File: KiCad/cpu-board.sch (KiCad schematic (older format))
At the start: 56 parts, among them CON1 BARREL_JACK, J1 Conn_FT245R, SW1 SW_PUSH_SMALL, SW2 SW_PUSH_SMALL, SW3 SWITCH_INV, U1 29F040B, U10 74LS377, U11 GAL22V10, U2 68008D, U3 74LS00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

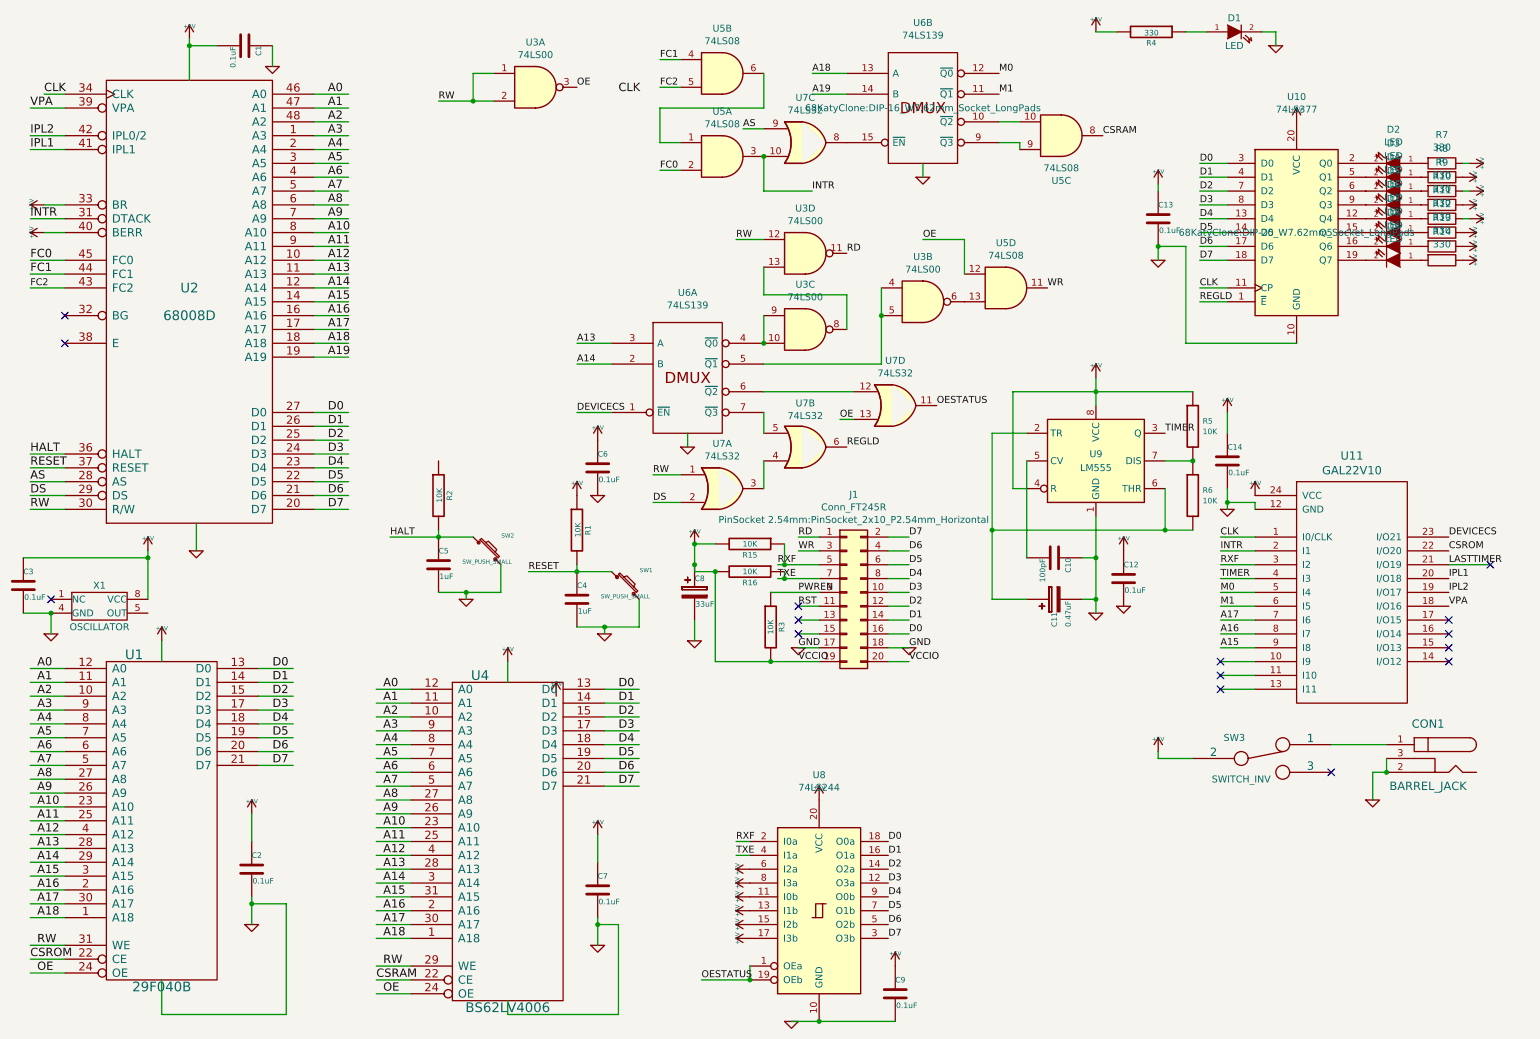
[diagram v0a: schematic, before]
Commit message: re-label active-low pins with bars
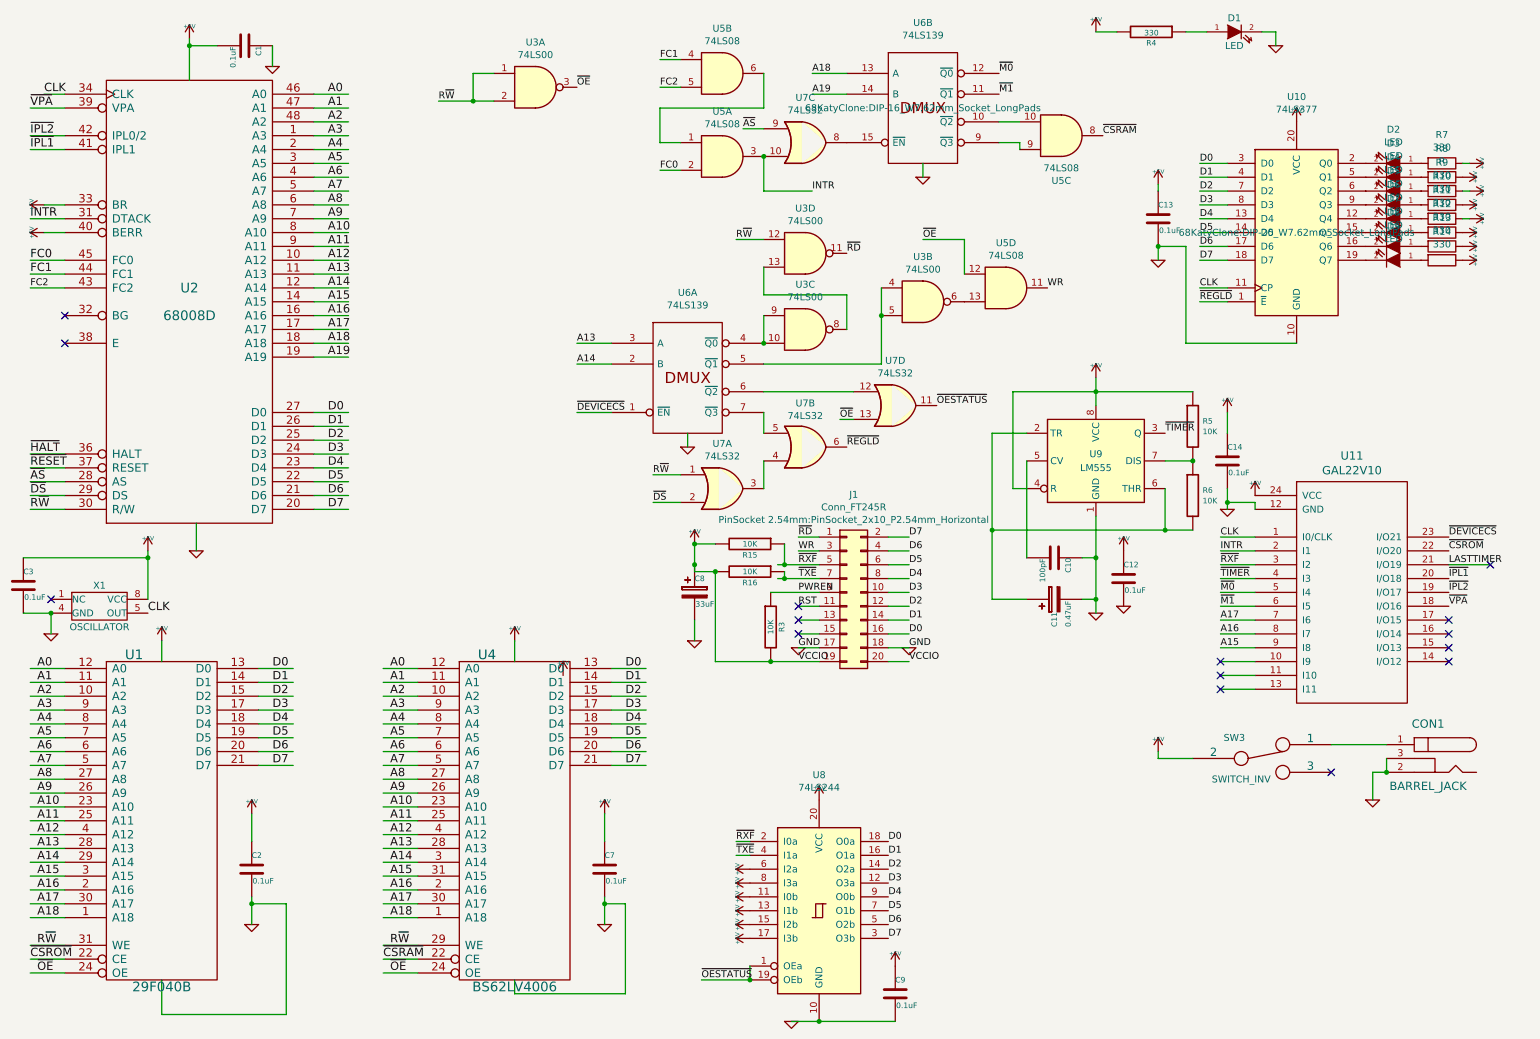
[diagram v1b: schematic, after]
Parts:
- removed C4, C5: 1uF, Discret:C1, symbol cpu-board-rescue:C
- removed C6: 0.1uF, Discret:C1, symbol cpu-board-rescue:C
- removed R1, R2: 10K, Discret:R3-5, symbol cpu-board-rescue:R
- removed SW1, SW2: SW_PUSH_SMALL, Discret:SW_PUSH_SMALL, symbol cpu-board-rescue:SW_PUSH_SMALL
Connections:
- net labels added: R~W, ~AS, ~CSRAM, ~CSROM, ~DEVICECS, ~DS, ~HALT, ~IPL1, ~IPL2, ~M0, ~M1, ~OE, ~OESTATUS, ~RD, ~REGLD, ~RESET, ~RXF, ~TIMER, ~TXE, ~VPA
- net labels removed: AS, CSRAM, CSROM, DEVICECS, DS, HALT, IPL1, IPL2, M0, M1, OE, OESTATUS, RD, REGLD, RESET, RW, RXF, TIMER, TXE, VPA
- wire segments 286 -> 272
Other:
- moved on the sheet: C7, U4

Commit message: remove data bus LEDs, they are of little use
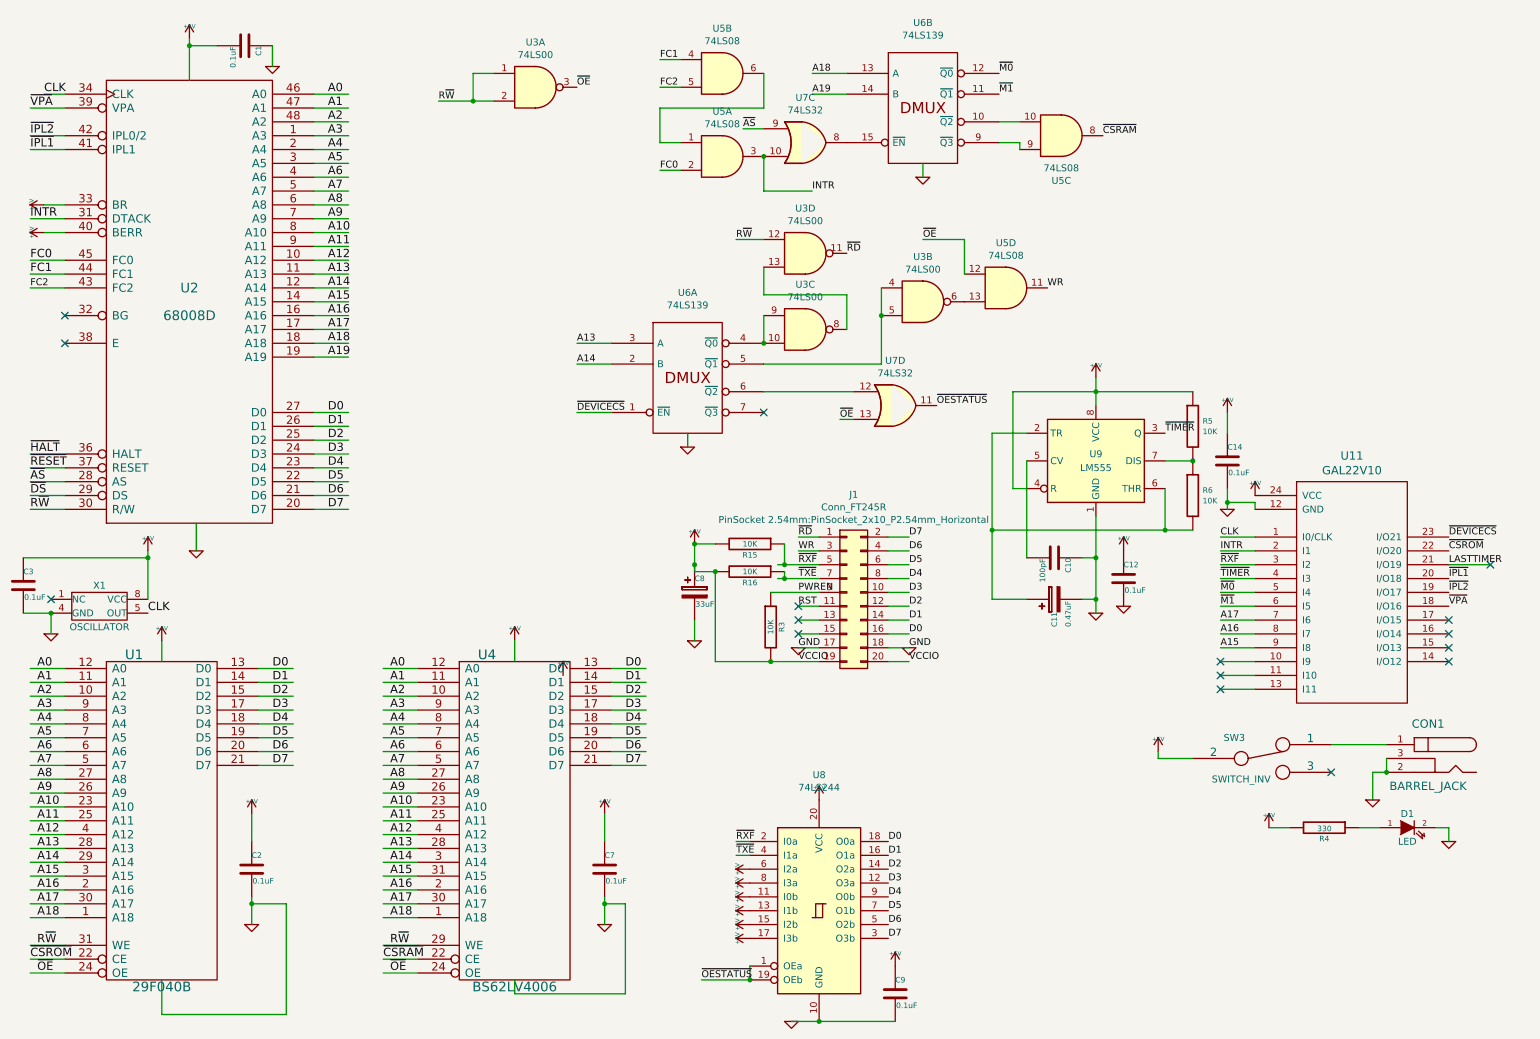
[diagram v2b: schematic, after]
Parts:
- removed C13: 0.1uF, Discret:C1, symbol cpu-board-rescue:C
- removed D2, D3, D4, D5, D6, D7, D8, D9: LED, symbol cpu-board-rescue:LED
- removed R10, R11, R12, R13, R14, R7, R9: 330, symbol Device:R
- removed R8: R, symbol Device:R
- removed U10: 74LS377, 68KatyClone:DIP-20_W7.62mm_Socket_LongPads, symbol 74xx:74LS377
- removed unit 2 of U7
- removed unit 1 of U7
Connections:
- net labels removed: ~REGLD
- wire segments 272 -> 250
- no-connect marks 15 -> 16
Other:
- moved on the sheet: D1, R4

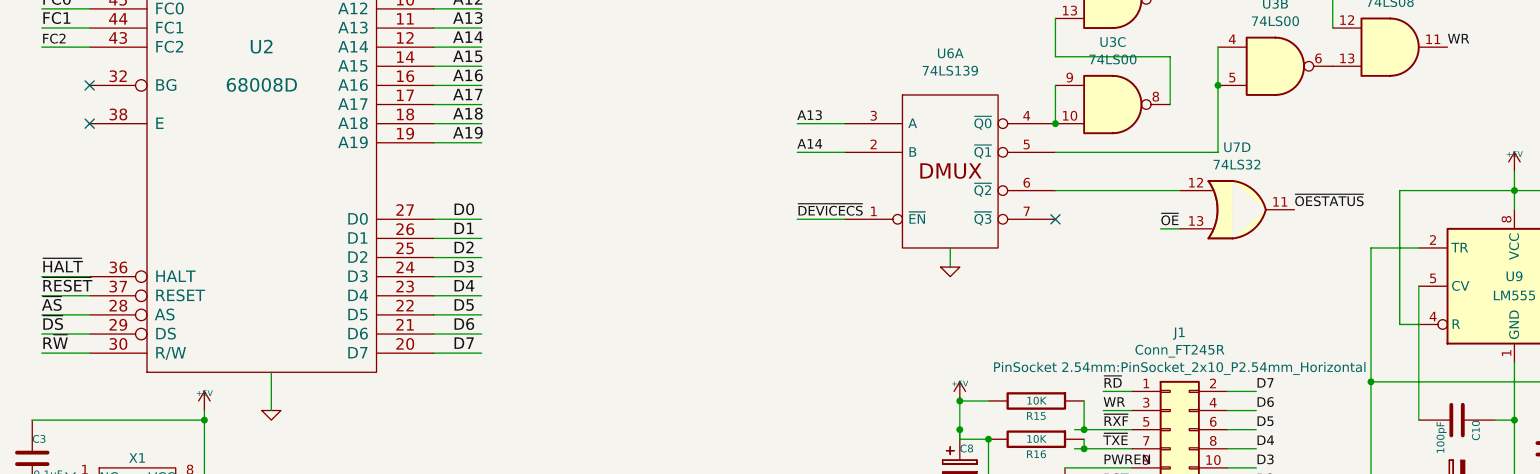
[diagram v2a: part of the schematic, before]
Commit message: disconnect unused data strobe line
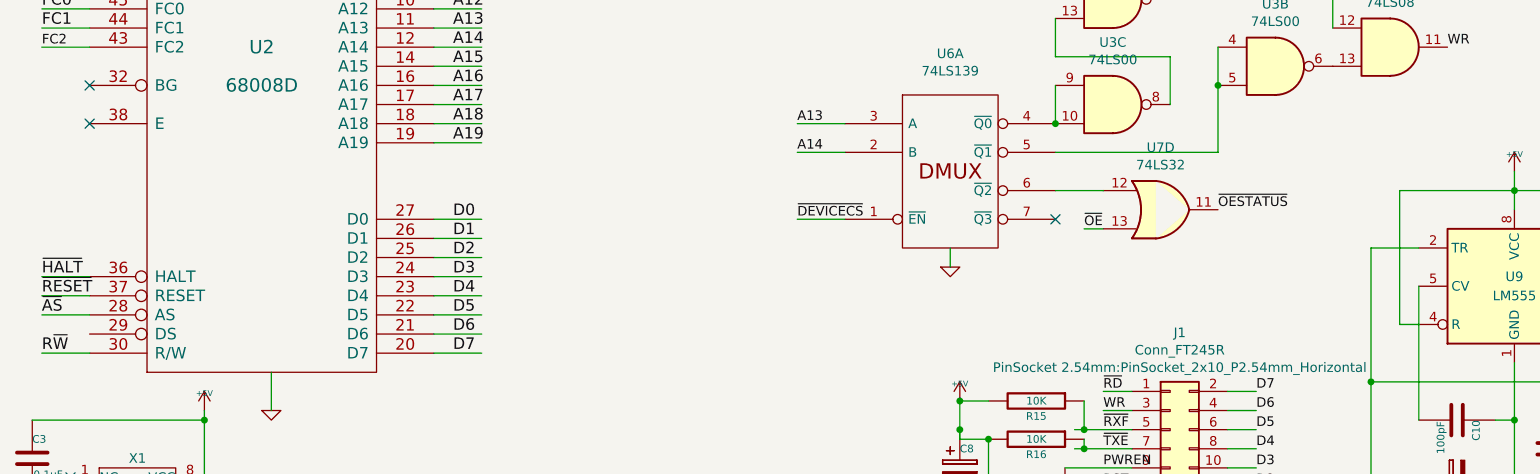
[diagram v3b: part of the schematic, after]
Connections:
- net labels removed: ~DS
- wire segments 250 -> 249
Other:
- moved on the sheet: U7D
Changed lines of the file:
@@
 Text Label 600  3850 0    60   ~ 0
 ~AS
-Text Label 600  3950 0    60   ~ 0
-~DS
 Wire Wire Line
 	2650 3350 2900 3350
@@
 	600  3850 850  3850
 Wire Wire Line
-	600  3950 850  3950
-Wire Wire Line
 	10400 5850 10400 5950
 Wire Wire Line
@@
 	1    0    0    -1
 $EndComp
-$Comp
-L 74xx:74LS32 U7
-U 4 1 5E16F553
-P 6850 3300
-F 0 "U7" H 6850 3625 50  0000 C CNN
-F 1 "74LS32" H 6850 3534 50  0000 C CNN
-F 2 "68KatyClone:DIP-14_W7.62mm_Socket_LongPads" H 6850 3300 50  0001 C CNN
-F 3 "http://www.ti.com/lit/gpn/sn74LS32" H 6850 3300 50  0001 C CNN
-	4    6850 3300
-	1    0    0    -1
-$EndComp
-Text Label 6450 3400 0    50   ~ 0
-~OE
-Text Label 7150 3300 0    50   ~ 0
-~OESTATUS
 Wire Wire Line
 	600  2450 850  2450
@@
 Connection ~ 6750 2650
 Wire Wire Line
-	5900 3200 6550 3200
-Wire Wire Line
-	6450 3400 6550 3400
-Wire Wire Line
 	6750 2650 6750 3000
 Wire Wire Line
@@
 INTR
 NoConn ~ 5900 3350
+Wire Wire Line
+	6050 3400 6150 3400
+Text Label 6750 3300 0    50   ~ 0
+~OESTATUS
+Text Label 6050 3400 0    50   ~ 0
+~OE
+$Comp
+L 74xx:74LS32 U7
+U 4 1 5E16F553
+P 6450 3300
+F 0 "U7" H 6450 3625 50  0000 C CNN
+F 1 "74LS32" H 6450 3534 50  0000 C CNN
+F 2 "68KatyClone:DIP-14_W7.62mm_Socket_LongPads" H 6450 3300 50  0001 C CNN
+F 3 "http://www.ti.com/lit/gpn/sn74LS32" H 6450 3300 50  0001 C CNN
+	4    6450 3300
+	1    0    0    -1
+$EndComp
+Wire Wire Line
+	5900 3200 6150 3200
 $EndSCHEMATC
